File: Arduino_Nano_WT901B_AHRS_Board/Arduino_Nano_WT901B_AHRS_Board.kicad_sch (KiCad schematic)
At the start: 9 parts, among them J1 Conn_01x04, J1 Conn_01x09_Pin, J4 Conn_01x02_Pin, J4 SolderPad1, J5 Conn_01x02_Pin, J6 OSTTC022162, J7 SolderPad2

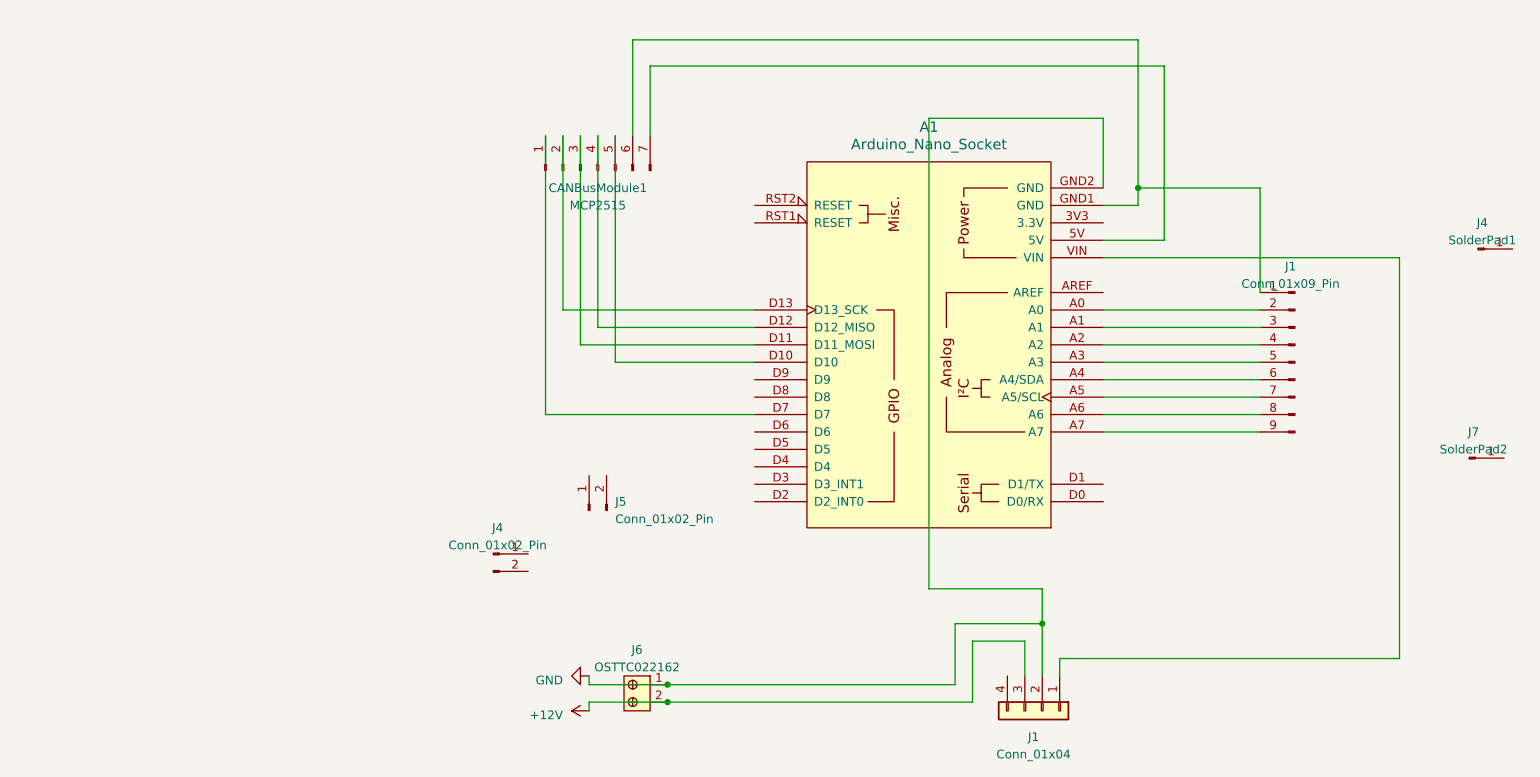
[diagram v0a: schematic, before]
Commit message: Created a new board for the Wit-Motion WT901B IMU chip.
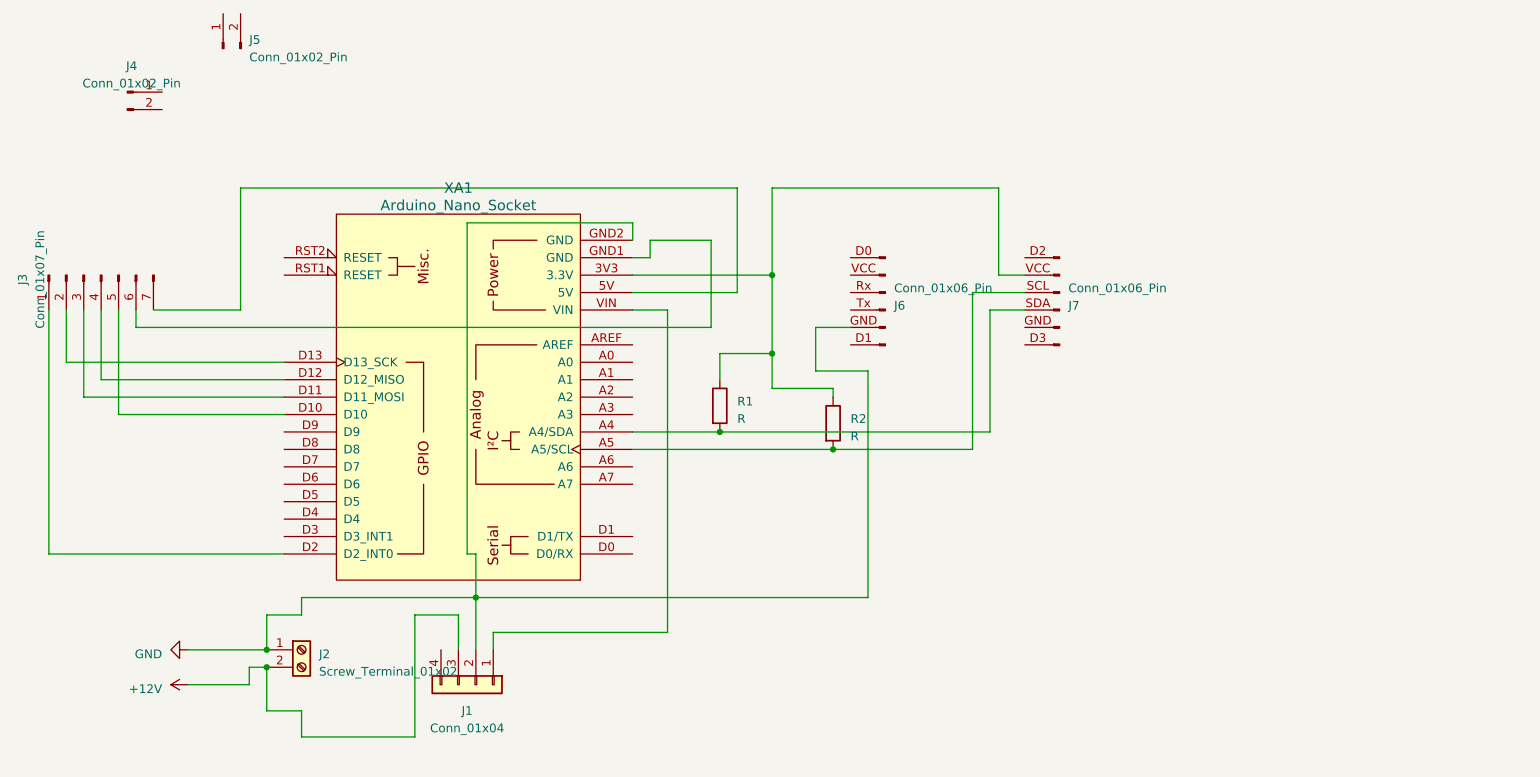
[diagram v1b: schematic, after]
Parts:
- removed A1: Arduino_Nano_Socket, PCM_arduino-library:Arduino_Nano_Socket, symbol PCM_arduino-library:Arduino_Nano_Socket
- removed CANBusModule1: MCP2515, Connector_PinHeader_2.54mm:PinHeader_1x07_P2.54mm_Vertical, symbol Connector:Conn_01x07_Pin
- removed J1: Conn_01x09_Pin, Connector_PinHeader_2.54mm:PinHeader_1x09_P2.54mm_Horizontal, symbol Connector:Conn_01x09_Pin
- removed J4: SolderPad1, TestPoint:TestPoint_Pad_D4.0mm, symbol Connector:Conn_01x01_Pin
- removed J6: OSTTC022162, digikey-footprints:Term_Block_1x2_P5.08MM, symbol dk_Terminal-Blocks-Wire-to-Board:OSTTC022162
- removed J7: SolderPad2, TestPoint:TestPoint_Pad_D4.0mm, symbol Connector:Conn_01x01_Pin
- added J2: Screw_Terminal_01x02, TerminalBlock:TerminalBlock_bornier-2_P5.08mm, symbol Connector:Screw_Terminal_01x02
- added J3: Conn_01x07_Pin, Library:PinHeader_1x07_P2.54mm_Vertical, symbol Connector:Conn_01x07_Pin
- added J6, J7: Conn_01x06_Pin, Connector_PinHeader_2.54mm:PinHeader_1x06_P2.54mm_Vertical, symbol Connector:Conn_01x06_Pin
- added R1, R2: R, Resistor_THT:R_Axial_DIN0204_L3.6mm_D1.6mm_P7.62mm_Horizontal, symbol Device:R
- added XA1: Arduino_Nano_Socket, Library:Arduino_Nano_Socket, symbol arduino-library:Arduino_Nano_Socket
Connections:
- net +12V: now also J2.2 (Pin_2)
- net GND: now also J2.1 (Pin_1), J6.GND (Pin_5), XA1.GND2 (GND)
- net at J1.1 (Pin_1): now also XA1.VIN
- new net: J7.VCC (Pin_2), R1.1, R2.1, XA1.3V3 (3.3V)
- new net: J7.SDA (Pin_4), R1.2, XA1.A4 (A4/SDA)
- new net: J3.7 (Pin_7), XA1.5V
- new net: J7.SCL (Pin_3), R2.2, XA1.A5 (A5/SCL)
- new net: J3.5 (Pin_5), XA1.D10
- new net: J3.3 (Pin_3), XA1.D11 (D11_MOSI)
- new net: J3.4 (Pin_4), XA1.D12 (D12_MISO)
- new net: J3.2 (Pin_2), XA1.D13 (D13_SCK)
- new net: J3.1 (Pin_1), XA1.D2 (D2_INT0)
- new net: J3.6 (Pin_6), XA1.GND1 (GND)
